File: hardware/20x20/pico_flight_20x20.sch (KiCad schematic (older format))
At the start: 45 parts, among them J1 USB_B_Micro, J2 Conn_01x02, J3 DEBUG, J4 ESC_AIKON32, J5 UART1, J6 UART2, J7 CAM, J8 VTX, U1 MCP1711T-33I_OT, U2 W25Q128JVS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

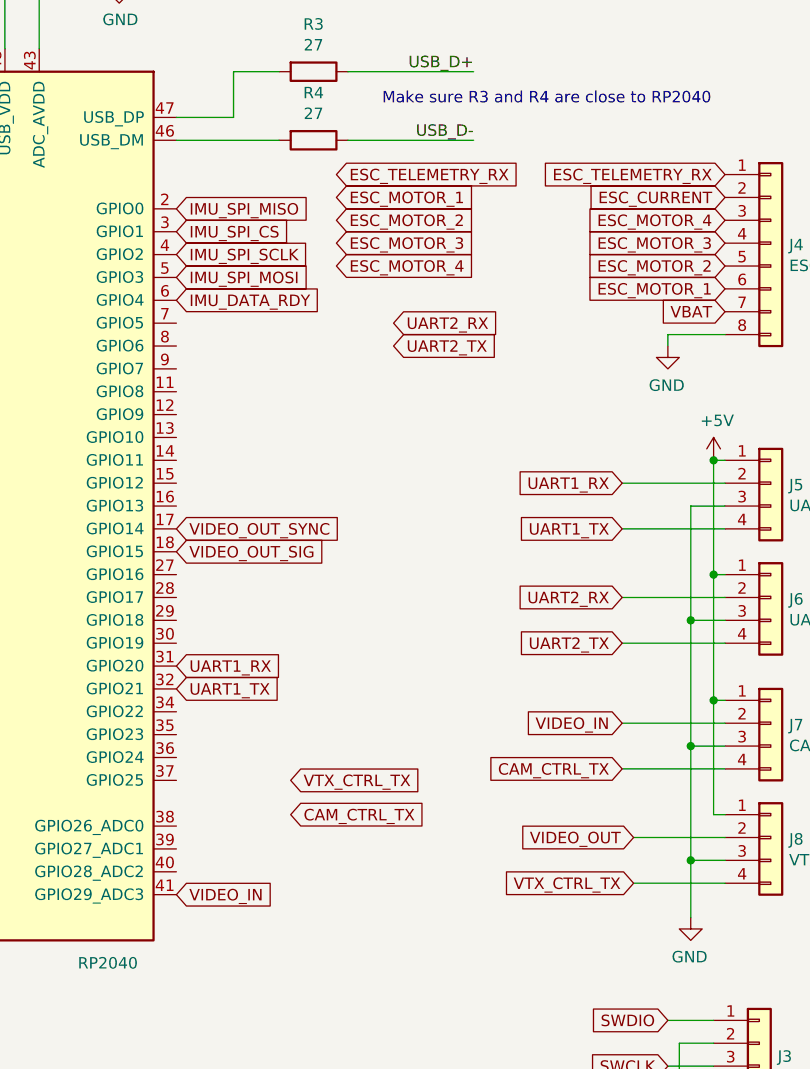
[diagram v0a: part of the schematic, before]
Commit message: Add implot, test mahi-gui, progress on pcb
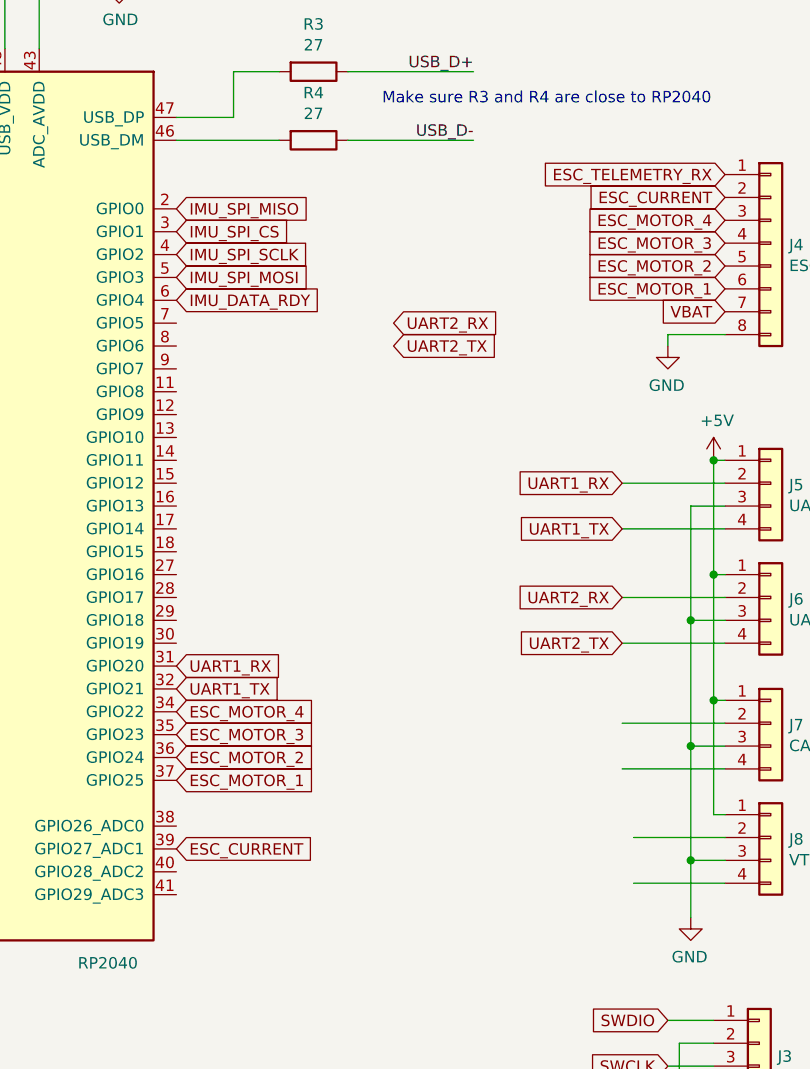
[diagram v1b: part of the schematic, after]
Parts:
- C18, C19, C2, C20, C3: footprint Capacitor_SMD:C_0603_1608Metric -> Capacitor_SMD:C_0402_1005Metric
- R1, R2: footprint Capacitor_SMD:C_0402_1005Metric -> Capacitor_SMD:C_0603_1608Metric
- R3, R4, R5: footprint Capacitor_SMD:C_0402_1005Metric -> Resistor_SMD:R_0402_1005Metric
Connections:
- net ESC_CURRENT: now also U3.39 (GPIO27_ADC1)
- net ESC_MOTOR_1: now also U3.37 (GPIO25)
- net ESC_MOTOR_2: now also U3.36 (GPIO24)
- net ESC_MOTOR_3: now also U3.35 (GPIO23)
- net ESC_MOTOR_4: now also U3.34 (GPIO22)
- net CAM_CTRL_TX: no longer names the net of J7.4 (Pin_4)
- net VIDEO_IN: no longer names the net of U3.41 (GPIO29_ADC3)
- net VIDEO_IN: no longer J7.2 (Pin_2)
- net VIDEO_OUT: no longer names the net of J8.2 (Pin_2)
- net VIDEO_OUT_SIG: no longer names the net of U3.18 (GPIO15)
- net VIDEO_OUT_SYNC: no longer names the net of U3.17 (GPIO14)
- net VTX_CTRL_TX: no longer names the net of J8.4 (Pin_4)
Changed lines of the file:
@@
 F 0 "C2" H 2115 8546 50  0000 L CNN
 F 1 "27p" H 2115 8455 50  0000 L CNN
-F 2 "Capacitor_SMD:C_0603_1608Metric" H 2038 8350 50  0001 C CNN
+F 2 "Capacitor_SMD:C_0402_1005Metric" H 2038 8350 50  0001 C CNN
 F 3 "~" H 2000 8500 50  0001 C CNN
 	1    2000 8500
@@
 F 0 "C3" H 2115 9046 50  0000 L CNN
 F 1 "27p" H 2115 8955 50  0000 L CNN
-F 2 "Capacitor_SMD:C_0603_1608Metric" H 2038 8850 50  0001 C CNN
+F 2 "Capacitor_SMD:C_0402_1005Metric" H 2038 8850 50  0001 C CNN
 F 3 "~" H 2000 9000 50  0001 C CNN
 	1    2000 9000
@@
 F 0 "R4" V 9443 4100 50  0000 C CNN
 F 1 "27" V 9534 4100 50  0000 C CNN
-F 2 "Capacitor_SMD:C_0402_1005Metric" V 9580 4100 50  0001 C CNN
+F 2 "Resistor_SMD:R_0402_1005Metric" V 9580 4100 50  0001 C CNN
 F 3 "~" H 9650 4100 50  0001 C CNN
 	1    9650 4100
@@
 F 0 "R1" V 1493 6700 50  0000 C CNN
 F 1 "1k" V 1584 6700 50  0000 C CNN
-F 2 "Capacitor_SMD:C_0402_1005Metric" V 1630 6700 50  0001 C CNN
+F 2 "Capacitor_SMD:C_0603_1608Metric" V 1630 6700 50  0001 C CNN
 F 3 "~" H 1700 6700 50  0001 C CNN
 	1    1700 6700
@@
 F 0 "R2" H 2370 6146 50  0000 L CNN
 F 1 "DNF" H 2370 6055 50  0000 L CNN
-F 2 "Capacitor_SMD:C_0402_1005Metric" V 2230 6100 50  0001 C CNN
+F 2 "Capacitor_SMD:C_0603_1608Metric" V 2230 6100 50  0001 C CNN
 F 3 "~" H 2300 6100 50  0001 C CNN
 	1    2300 6100
@@
 F 0 "R3" V 9443 3800 50  0000 C CNN
 F 1 "27" V 9534 3800 50  0000 C CNN
-F 2 "Capacitor_SMD:C_0402_1005Metric" V 9580 3800 50  0001 C CNN
+F 2 "Resistor_SMD:R_0402_1005Metric" V 9580 3800 50  0001 C CNN
 F 3 "~" H 9650 3800 50  0001 C CNN
 	1    9650 3800
@@
 F 0 "R5" V 3093 9000 50  0000 C CNN
 F 1 "1k" V 3184 9000 50  0000 C CNN
-F 2 "Capacitor_SMD:C_0402_1005Metric" V 3230 9000 50  0001 C CNN
+F 2 "Resistor_SMD:R_0402_1005Metric" V 3230 9000 50  0001 C CNN
 F 3 "~" H 3300 9000 50  0001 C CNN
 	1    3300 9000
@@
 F 0 "C18" H 14315 946 50  0000 L CNN
 F 1 "10nF" H 14315 855 50  0000 L CNN
-F 2 "Capacitor_SMD:C_0603_1608Metric" H 14238 750 50  0001 C CNN
+F 2 "Capacitor_SMD:C_0402_1005Metric" H 14238 750 50  0001 C CNN
 F 3 "~" H 14200 900 50  0001 C CNN
 	1    14200 900
@@
 F 0 "C19" H 14715 946 50  0000 L CNN
 F 1 "0.1uF" H 14715 855 50  0000 L CNN
-F 2 "Capacitor_SMD:C_0603_1608Metric" H 14638 750 50  0001 C CNN
+F 2 "Capacitor_SMD:C_0402_1005Metric" H 14638 750 50  0001 C CNN
 F 3 "~" H 14600 900 50  0001 C CNN
 	1    14600 900
@@
 F 0 "C20" H 15565 2346 50  0000 L CNN
 F 1 "0.1uF" H 15565 2255 50  0000 L CNN
-F 2 "Capacitor_SMD:C_0603_1608Metric" H 15488 2150 50  0001 C CNN
+F 2 "Capacitor_SMD:C_0402_1005Metric" H 15488 2150 50  0001 C CNN
 F 3 "~" H 15450 2300 50  0001 C CNN
 	1    15450 2300
@@
 Wire Wire Line
 	11300 6200 11300 6750
-Text GLabel 11050 7350 0    50   Input ~ 0
-VTX_CTRL_TX
-Text GLabel 11050 7150 0    50   Input ~ 0
-VIDEO_OUT
-Text GLabel 11000 6650 0    50   Input ~ 0
-VIDEO_IN
-Text GLabel 11000 6850 0    50   Input ~ 0
-CAM_CTRL_TX
 Wire Wire Line
 	11000 6650 11450 6650
@@
 Text Notes 14100 650  0    50   ~ 0
 MPU-9250
-Text GLabel 9750 4250 2    50   Input ~ 0
-ESC_TELEMETRY_RX
-Text GLabel 9750 4350 2    50   Input ~ 0
+Text GLabel 9050 6900 2    50   Input ~ 0
 ESC_MOTOR_1
-Text GLabel 9750 4450 2    50   Input ~ 0
+Text GLabel 9050 6800 2    50   Input ~ 0
 ESC_MOTOR_2
-Text GLabel 9750 4550 2    50   Input ~ 0
+Text GLabel 9050 6700 2    50   Input ~ 0
 ESC_MOTOR_3
-Text GLabel 9750 4650 2    50   Input ~ 0
+Text GLabel 9050 6600 2    50   Input ~ 0
 ESC_MOTOR_4
-Text GLabel 9550 6900 2    50   Input ~ 0
-VTX_CTRL_TX
-Text GLabel 9050 5800 2    50   Input ~ 0
-VIDEO_OUT_SYNC
-Text GLabel 9050 7400 2    50   Input ~ 0
-VIDEO_IN
-Text GLabel 9550 7050 2    50   Input ~ 0
-CAM_CTRL_TX
 Text GLabel 9050 6400 2    50   Input ~ 0
 UART1_RX
@@
 Text GLabel 9050 4800 2    50   Input ~ 0
 IMU_DATA_RDY
-Text GLabel 9050 5900 2    50   Input ~ 0
-VIDEO_OUT_SIG
 Wire Wire Line
 	3350 3100 3350 3150
@@
 	1    0    0    -1
 $EndComp
+Text GLabel 9050 7200 2    50   Input ~ 0
+ESC_CURRENT
 $EndSCHEMATC

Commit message: latest board
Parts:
- J5: footprint Connector_PinHeader_1.00mm:PinHeader_1x04_P1.00mm_Vertical -> pico-flight:PAD_X4_SMD_03x02
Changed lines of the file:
@@
 F 0 "J5" H 11730 5592 50  0000 L CNN
 F 1 "UART1" H 11730 5501 50  0000 L CNN
-F 2 "Connector_PinHeader_1.00mm:PinHeader_1x04_P1.00mm_Vertical" H 11730 5455 50  0001 L CNN
+F 2 "pico-flight:PAD_X4_SMD_03x02" H 11730 5455 50  0001 L CNN
 F 3 "~" H 11650 5600 50  0001 C CNN
 	1    11650 5600
